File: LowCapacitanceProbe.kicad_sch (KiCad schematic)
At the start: 40 parts, among them J2 SMA, J3 Barrel_Jack_Switch, Q1 BF998, U2 SPX3819M5-L-5-0

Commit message: Added footprint and model of P50 broken needle and whole pogo with sleeve. Finalizing shape and ground contacts.
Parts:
- TP1: footprint Connector_PinHeader_1.00mm:PinHeader_1x01_P1.00mm_Horizontal -> petr:P50-B1_needle
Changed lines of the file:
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@@
 			)
 		)
-		(property "Footprint" "Connector_PinHeader_1.00mm:PinHeader_1x01_P1.00mm_Horizontal"
+		(property "Footprint" "petr:P50-B1_needle"
 			(at 93.98 113.03 0)
 			(effects

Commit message: Some macdinking, review/checklist in progress.
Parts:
- J2: value SMA -> OUTPUT
- J3: value Barrel_Jack_Switch -> POWER IN
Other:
- note added: "6 ... 16 V << 50 mA LOW NOISE!"
- note added: "The resistor protects external gear from damage! Its assembly is mandatory! Make sure that ext. gear does not present voltage >10 V."
- note removed: "6 ... 16 V"
- note removed: "The resistor protects external gear from damage! Its assembly is mandatory!"
- company: (none) -> Author: Petr Polášek
- title: (none) -> Low Capacitance (<1 pF) 10:1 AC 1+ GHz Probe
- moved on the sheet: D3, J3, R20

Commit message: Final finishing touches, checking.
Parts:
- added SYM1: Logo_Open_Hardware_Small, Symbol:OSHW-Logo2_7.3x6mm_SilkScreen, symbol Graphic:Logo_Open_Hardware_Small
- added SYM3: SYM_ESD_Large, Symbol:ESD-Logo_6.6x6mm_SilkScreen, symbol Graphic:SYM_ESD_Large
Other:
- company: Author: Petr Polášek -> Author: ${Author}

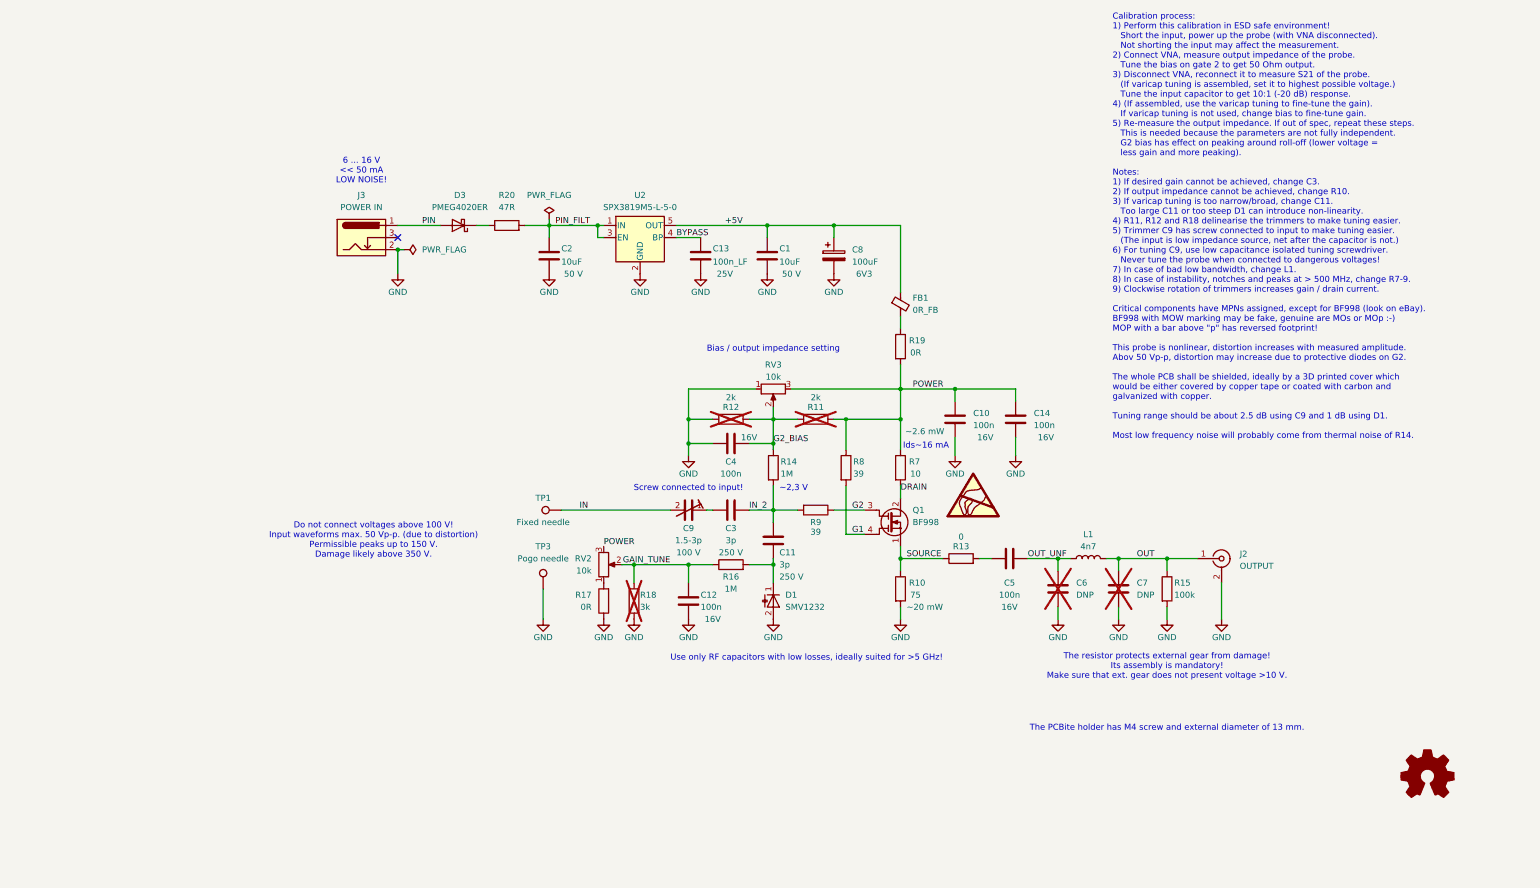
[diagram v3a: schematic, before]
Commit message: Finishing PCB, toying with jobset, exporting data.
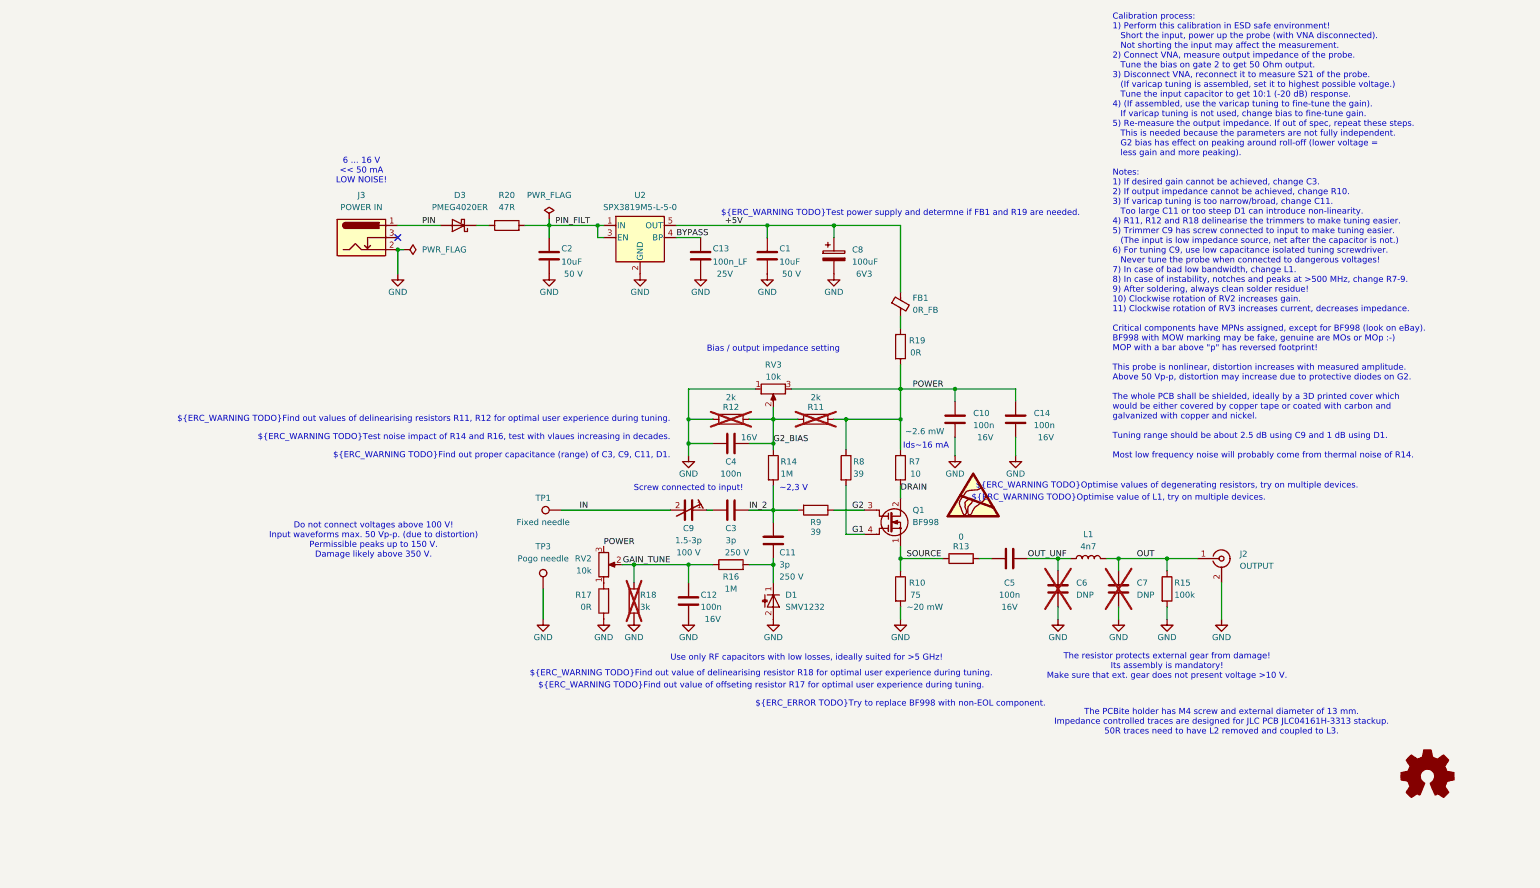
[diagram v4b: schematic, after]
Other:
- note added: "${ERC_ERROR TODO}Try to replace BF998 with non-EOL component."
- note added: "${ERC_WARNING TODO}Find out proper capacitance (range) of C3, C9, C11, D1."
- note added: "${ERC_WARNING TODO}Find out value of delinearising resistor R18 for optimal user experience during tuning."
- note added: "${ERC_WARNING TODO}Find out value of offseting resistor R17 for optimal user experience during tuning."
- note added: "${ERC_WARNING TODO}Find out values of delinearising resistors R11, R12 for optimal user experience during tuning."
- note added: "${ERC_WARNING TODO}Optimise value of L1, try on multiple devices."
- note added: "${ERC_WARNING TODO}Optimise values of degenerating resistors, try on multiple devices."
- note added: "${ERC_WARNING TODO}Test noise impact of R14 and R16, test with vlaues increasing in decades."
- note added: "${ERC_WARNING TODO}Test power supply and determne if FB1 and R19 are needed."
- note added: "The PCBite holder has M4 screw and external diameter of 13 mm. Impedance controlled traces are designed for JLC PCB JLC04161H-3313 stackup. 50R traces need to have L2 removed and coupled to L3."
- note removed: "The PCBite holder has M4 screw and external diameter of 13 mm."
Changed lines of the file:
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@@
 		(company "Author: ${Author}")
 	)
+	(text "${ERC_WARNING TODO}Test noise impact of R14 and R16, test with vlaues increasing in decades."
+		(exclude_from_sim no)
+		(at 116.84 102.87 0)
+		(effects
+			(font
+				(size 1.27 1.27)
+				(color 255 135 0 1)
+			)
+			(justify right)
+		)
+	)
 	(text "Do not connect voltages above 100 V!\nInput waveforms max. 50 Vp-p. (due to distortion)\nPermissible peaks up to 150 V.\nDamage likely above 350 V."
 		(exclude_from_sim no)
@@
 		)
 	)
+	(text "${ERC_WARNING TODO}Optimise value of L1, try on multiple devices."
+		(exclude_from_sim no)
+		(at 210.82 115.57 0)
+		(effects
+			(font
+				(size 1.27 1.27)
+				(color 255 135 0 1)
+			)
+		)
+	)
 	(text "Use only RF capacitors with low losses, ideally suited for >5 GHz!"
 		(exclude_from_sim no)
@@
 		)
 	)
+	(text "${ERC_WARNING TODO}Find out proper capacitance (range) of C3, C9, C11, D1."
+		(exclude_from_sim no)
+		(at 116.84 106.68 0)
+		(effects
+			(font
+				(size 1.27 1.27)
+				(color 255 135 0 1)
+			)
+			(justify right)
+		)
+	)
+	(text "${ERC_WARNING TODO}Find out value of offseting resistor R17 for optimal user experience during tuning."
+		(exclude_from_sim no)
+		(at 135.89 154.94 0)
+		(effects
+			(font
+				(size 1.27 1.27)
+				(color 255 135 0 1)
+			)
+		)
+	)
+	(text "${ERC_WARNING TODO}Find out values of delinearising resistors R11, R12 for optimal user experience during tuning."
+		(exclude_from_sim no)
+		(at 116.84 99.06 0)
+		(effects
+			(font
+				(size 1.27 1.27)
+				(color 255 135 0 1)
+			)
+			(justify right)
+		)
+	)
 	(text "~2,3 V"
 		(exclude_from_sim no)
@@
 		)
 	)
-	(text "Calibration process:\n1) Perform this calibration in ESD safe environment!\n   Short the input, power up the probe (with VNA disconnected).\n   Not shorting the input may affect the measurement.\n2) Connect VNA, measure output impedance of the probe.\n   Tune the bias on gate 2 to get 50 Ohm output.\n3) Disconnect VNA, reconnect it to measure S21 of the probe.\n   (If varicap tuning is assembled, set it to highest possible voltage.)\n   Tune the input capacitor to get 10:1 (-20 dB) response.\n4) (If assembled, use the varicap tuning to fine-tune the gain).\n   If varicap tuning is not used, change bias to fine-tune gain.\n5) Re-measure the output impedance. If out of spec, repeat these steps.\n   This is needed because the parameters are not fully independent.\n   G2 bias has effect on peaking around roll-off (lower voltage = \n   less gain and more peaking).\n   \nNotes:\n1) If desired gain cannot be achieved, change C3.\n2) If output impedance cannot be achieved, change R10.\n3) If varicap tuning is too narrow/broad, change C11.\n   Too large C11 or too steep D1 can introduce non-linearity.\n4) R11, R12 and R18 delinearise the trimmers to make tuning easier.\n5) Trimmer C9 has screw connected to input to make tuning easier.\n   (The input is low impedance source, net after the capacitor is not.)\n6) For tuning C9, use low capacitance isolated tuning screwdriver.\n   Never tune the probe when connected to dangerous voltages!\n7) In case of bad low bandwidth, change L1.\n8) In case of instability, notches and peaks at > 500 MHz, change R7-9.\n9) Clockwise rotation of trimmers increases gain / drain current.\n\nCritical components have MPNs assigned, except for BF998 (look on eBay).\nBF998 with MOW marking may be fake, genuine are MOs or MOp :-)\nMOP with a bar above \"p\" has reversed footprint!\n\nThis probe is nonlinear, distortion increases with measured amplitude.\nAbov 50 Vp-p, distortion may increase due to protective diodes on G2.\n\nThe whole PCB shall be shielded, ideally by a 3D printed cover which\nwould be either covered by copper tape or coated with carbon and\ngalvanized with copper.\n\nTuning range should be about 2.5 dB using C9 and 1 dB using D1.\n\nMost low frequency noise will probably come from thermal noise of R14."
+	(text "Calibration process:\n1) Perform this calibration in ESD safe environment!\n   Short the input, power up the probe (with VNA disconnected).\n   Not shorting the input may affect the measurement.\n2) Connect VNA, measure output impedance of the probe.\n   Tune the bias on gate 2 to get 50 Ohm output.\n3) Disconnect VNA, reconnect it to measure S21 of the probe.\n   (If varicap tuning is assembled, set it to highest possible voltage.)\n   Tune the input capacitor to get 10:1 (-20 dB) response.\n4) (If assembled, use the varicap tuning to fine-tune the gain).\n   If varicap tuning is not used, change bias to fine-tune gain.\n5) Re-measure the output impedance. If out of spec, repeat these steps.\n   This is needed because the parameters are not fully independent.\n   G2 bias has effect on peaking around roll-off (lower voltage = \n   less gain and more peaking).\n   \nNotes:\n1) If desired gain cannot be achieved, change C3.\n2) If output impedance cannot be achieved, change R10.\n3) If varicap tuning is too narrow/broad, change C11.\n   Too large C11 or too steep D1 can introduce non-linearity.\n4) R11, R12 and R18 delinearise the trimmers to make tuning easier.\n5) Trimmer C9 has screw connected to input to make tuning easier.\n   (The input is low impedance source, net after the capacitor is not.)\n6) For tuning C9, use low capacitance isolated tuning screwdriver.\n   Never tune the probe when connected to dangerous voltages!\n7) In case of bad low bandwidth, change L1.\n8) In case of instability, notches and peaks at >500 MHz, change R7-9.\n9) After soldering, always clean solder residue!\n10) Clockwise rotation of RV2 increases gain.\n11) Clockwise rotation of RV3 increases current, decreases impedance.\n\nCritical components have MPNs assigned, except for BF998 (look on eBay).\nBF998 with MOW marking may be fake, genuine are MOs or MOp :-)\nMOP with a bar above \"p\" has reversed footprint!\n\nThis probe is nonlinear, distortion increases with measured amplitude.\nAbove 50 Vp-p, distortion may increase due to protective diodes on G2.\n\nThe whole PCB shall be shielded, ideally by a 3D printed cover which\nwould be either covered by copper tape or coated with carbon and\ngalvanized with copper and nickel.\n\nTuning range should be about 2.5 dB using C9 and 1 dB using D1.\n\nMost low frequency noise will probably come from thermal noise of R14."
 		(exclude_from_sim no)
 		(at 209.55 13.97 0)
@@
 		)
 	)
+	(text "${ERC_ERROR TODO}Try to replace BF998 with non-EOL component."
+		(exclude_from_sim no)
+		(at 165.1 158.75 0)
+		(effects
+			(font
+				(size 1.27 1.27)
+				(color 255 42 0 1)
+			)
+		)
+	)
+	(text "${ERC_WARNING TODO}Optimise values of degenerating resistors, try on multiple devices."
+		(exclude_from_sim no)
+		(at 220.98 113.03 0)
+		(effects
+			(font
+				(size 1.27 1.27)
+				(color 255 135 0 1)
+			)
+		)
+	)
+	(text "${ERC_WARNING TODO}Find out value of delinearising resistor R18 for optimal user experience during tuning."
+		(exclude_from_sim no)
+		(at 135.89 152.4 0)
+		(effects
+			(font
+				(size 1.27 1.27)
+				(color 255 135 0 1)
+			)
+		)
+	)
 	(text "Screw connected to input!"
 		(exclude_from_sim no)
@@
 		)
 	)
+	(text "${ERC_WARNING TODO}Test power supply and determne if FB1 and R19 are needed."
+		(exclude_from_sim no)
+		(at 165.1 55.88 0)
+		(effects
+			(font
+				(size 1.27 1.27)
+				(color 255 135 0 1)
+			)
+		)
+	)
 	(text "6 ... 16 V\n<< 50 mA\nLOW NOISE!"
 		(exclude_from_sim no)
@@
 		)
 	)
-	(text "The PCBite holder has M4 screw and external diameter of 13 mm."
+	(text "The PCBite holder has M4 screw and external diameter of 13 mm.\nImpedance controlled traces are designed for JLC PCB JLC04161H-3313 stackup.\n50R traces need to have L2 removed and coupled to L3."
 		(exclude_from_sim no)
-		(at 220.98 163.83 0)
+		(at 232.41 162.56 0)
 		(effects
 			(font
@@
 		(polyline
 			(pts
-				(xy 82.55 111.76) (xy 133.35 111.76) (xy 135.89 109.22) (xy 171.45 109.22) (xy 171.45 116.84) (xy 160.02 116.84)
-				(xy 160.02 137.16) (xy 137.16 137.16) (xy 123.19 123.19) (xy 82.55 123.19)
+				(xy 162.56 134.62) (xy 227.33 134.62) (xy 227.33 121.92) (xy 167.64 121.92) (xy 162.56 127)
 			)
 			(stroke
@@
 			(fill
 				(type color)
-				(color 32 255 43 0.15)
+				(color 22 178 30 0.15)
 			)
 		)
@@
 		(polyline
 			(pts
-				(xy 162.56 134.62) (xy 227.33 134.62) (xy 227.33 121.92) (xy 167.64 121.92) (xy 162.56 127)
+				(xy 82.55 111.76) (xy 133.35 111.76) (xy 135.89 109.22) (xy 171.45 109.22) (xy 171.45 116.84) (xy 160.02 116.84)
+				(xy 160.02 137.16) (xy 137.16 137.16) (xy 123.19 123.19) (xy 82.55 123.19)
 			)
 			(stroke
@@
 			(fill
 				(type color)
-				(color 22 178 30 0.15)
+				(color 32 255 43 0.15)
 			)
 		)
@@
 		)
 		(property "Rating" "250 V"
-			(at 129.54 127 90)
+			(at 130.81 127 90)
 			(effects
 				(font

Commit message: Fixed some RF traces, copper fills, added some teardrops.
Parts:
- C1, C2: Rating (none) -> 50 V; voltage 50 V -> (none)
- C13: Rating (none) -> 25V; voltage 25V -> (none)
- C8: Rating (none) -> 6V3; voltage 6V3 -> (none)
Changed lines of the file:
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@@
 		(polyline
 			(pts
-				(xy 162.56 134.62) (xy 227.33 134.62) (xy 227.33 121.92) (xy 167.64 121.92) (xy 162.56 127)
+				(xy 82.55 111.76) (xy 133.35 111.76) (xy 135.89 109.22) (xy 171.45 109.22) (xy 171.45 116.84) (xy 160.02 116.84)
+				(xy 160.02 137.16) (xy 137.16 137.16) (xy 123.19 123.19) (xy 82.55 123.19)
 			)
 			(stroke
@@
 			(fill
 				(type color)
-				(color 22 178 30 0.15)
+				(color 32 255 43 0.15)
 			)
 		)
@@
 		(polyline
 			(pts
-				(xy 82.55 111.76) (xy 133.35 111.76) (xy 135.89 109.22) (xy 171.45 109.22) (xy 171.45 116.84) (xy 160.02 116.84)
-				(xy 160.02 137.16) (xy 137.16 137.16) (xy 123.19 123.19) (xy 82.55 123.19)
+				(xy 162.56 134.62) (xy 227.33 134.62) (xy 227.33 121.92) (xy 167.64 121.92) (xy 162.56 127)
 			)
 			(stroke
@@
 			(fill
 				(type color)
-				(color 32 255 43 0.15)
+				(color 22 178 30 0.15)
 			)
 		)
@@
 			)
 		)
-		(property "voltage" "50 V"
+		(property "Rating" "50 V"
 			(at 96.52 68.58 0)
 			(effects
@@
 			)
 		)
-		(property "voltage" "50 V"
+		(property "Rating" "50 V"
 			(at 142.24 68.58 0)
 			(effects
@@
 			)
 		)
-		(property "voltage" "25V"
+		(property "Rating" "25V"
 			(at 128.27 68.58 0)
 			(effects
@@
 			)
 		)
-		(property "voltage" "6V3"
+		(property "Rating" "6V3"
 			(at 157.48 68.58 0)
 			(effects
